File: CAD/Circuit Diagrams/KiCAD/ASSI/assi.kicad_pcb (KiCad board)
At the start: 2 copper layers, 38.1 x 76.2 mm, 24 parts, among them SW2 SW_Push, SW3 SW_Push

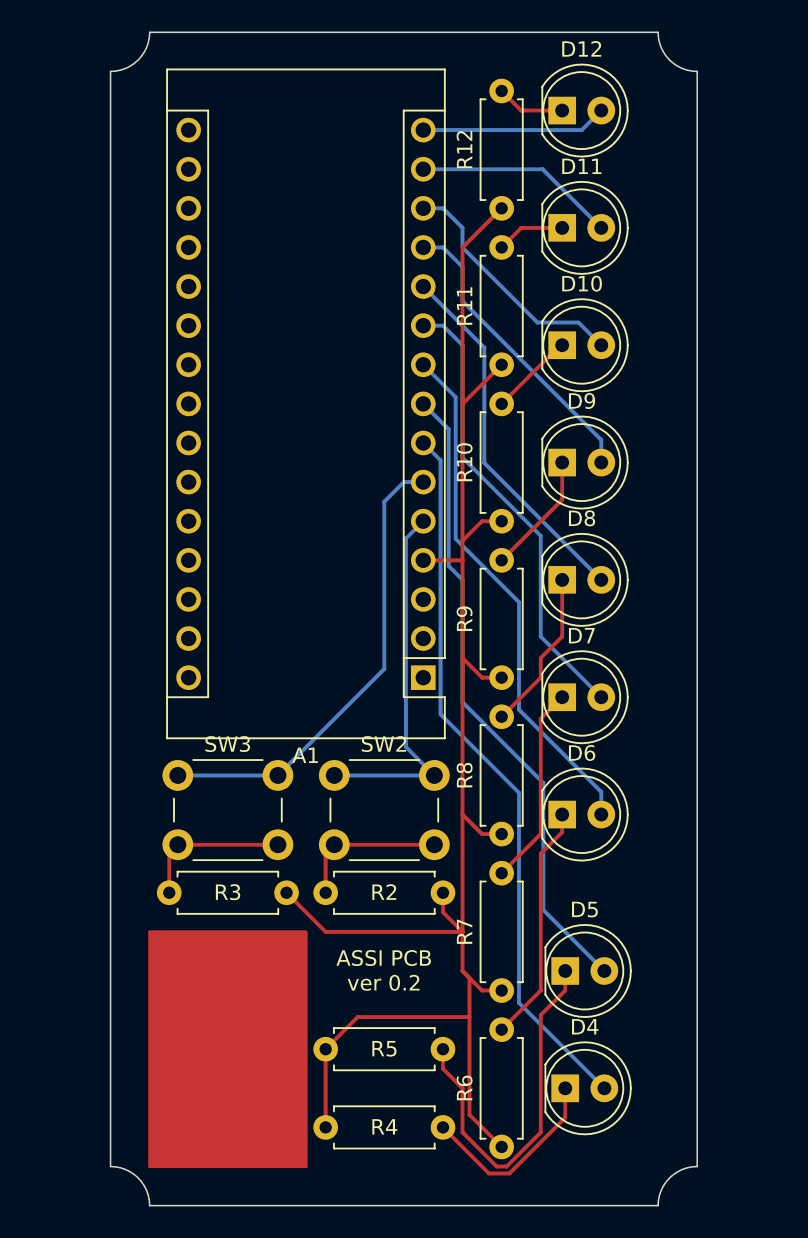
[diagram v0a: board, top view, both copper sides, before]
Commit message: ASSI PCB mountable
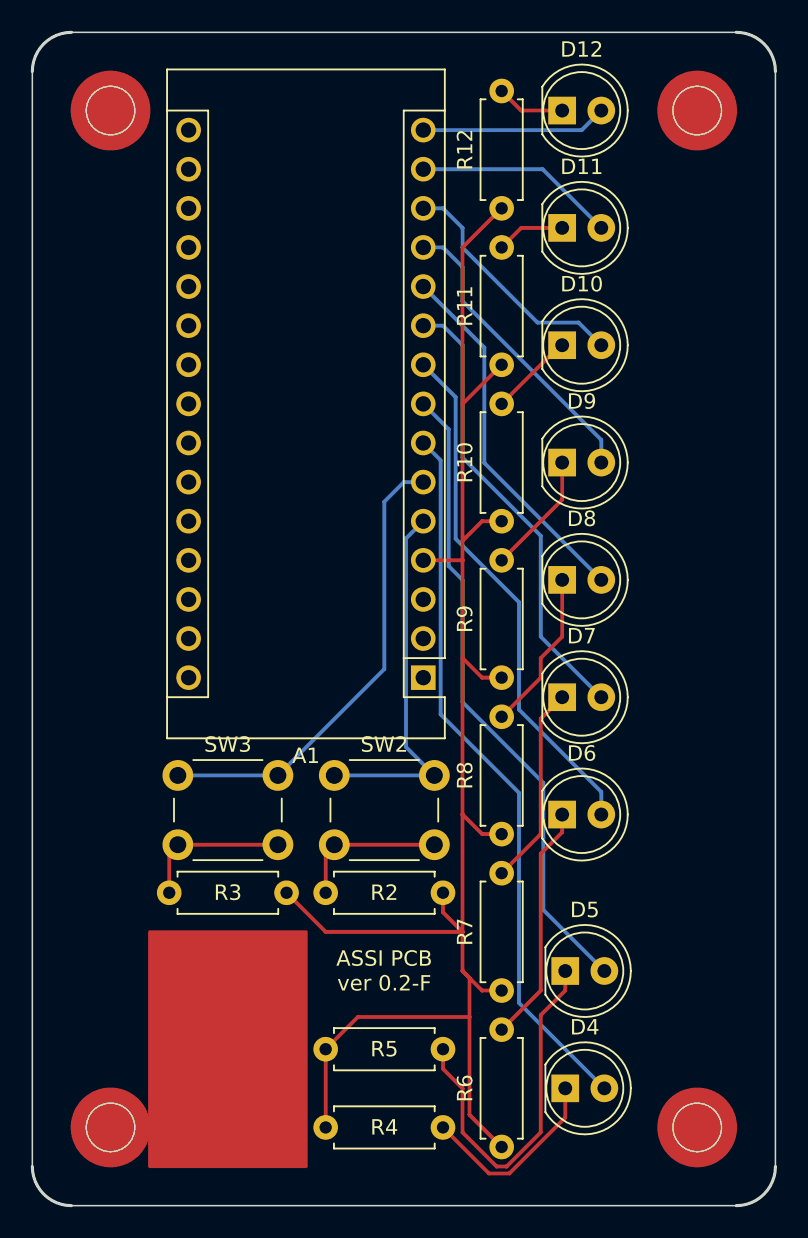
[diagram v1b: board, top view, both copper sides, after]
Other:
- board size 38.1 x 76.2 mm -> 48.3 x 76.2 mm
- board text added: "ASSI PCB ver 0.2-F"
- board text removed: "ASSI PCB ver 0.2"
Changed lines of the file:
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@@
   (setup
     (pad_to_mask_clearance 0)
-    (grid_origin 163.15 125.96)
+    (grid_origin 155.53 70.08)
     (pcbplotparams
       (layerselection 0x00010fc_ffffffff)
@@
     )
   )
+  (gr_circle (center 196.17 138.66) (end 198.71 138.66) (layer "F.Cu") (width 0.1) (fill solid))
+  (gr_circle (center 158.07 72.62) (end 160.61 72.62) (layer "F.Cu") (width 0.1) (fill solid))
   (gr_rect (start 160.61 125.96) (end 170.77 141.2) (layer "F.Cu") (width 0.2) (fill solid))
-  (gr_arc (start 196.17 70.08) (mid 194.373949 69.336051) (end 193.63 67.54) (layer "Edge.Cuts") (width 0.1))
-  (gr_line (start 193.63 67.54) (end 160.61 67.54) (layer "Edge.Cuts") (width 0.1))
-  (gr_arc (start 193.63 143.74) (mid 194.373949 141.943949) (end 196.17 141.2) (layer "Edge.Cuts") (width 0.1))
-  (gr_line (start 160.61 143.74) (end 193.63 143.74) (layer "Edge.Cuts") (width 0.1))
-  (gr_arc (start 160.61 67.54) (mid 159.866051 69.336051) (end 158.07 70.08) (layer "Edge.Cuts") (width 0.1))
-  (gr_line (start 196.17 141.2) (end 196.17 70.08) (layer "Edge.Cuts") (width 0.1))
-  (gr_arc (start 158.07 141.2) (mid 159.866051 141.943949) (end 160.61 143.74) (layer "Edge.Cuts") (width 0.1))
-  (gr_line (start 158.07 70.08) (end 158.07 141.2) (layer "Edge.Cuts") (width 0.1))
-  (gr_text "ASSI PCB\nver 0.2" (at 175.85 128.5) (layer "F.SilkS")
+  (gr_circle (center 196.17 72.62) (end 198.71 72.62) (layer "F.Cu") (width 0.1) (fill solid))
+  (gr_circle (center 158.07 138.66) (end 160.61 138.66) (layer "F.Cu") (width 0.1) (fill solid))
+  (gr_circle (center 196.17 138.66) (end 198.71 138.66) (layer "F.Paste") (width 0.1) (fill solid))
+  (gr_circle (center 158.07 138.66) (end 160.61 138.66) (layer "F.Paste") (width 0.1) (fill solid))
+  (gr_circle (center 158.07 72.62) (end 160.61 72.62) (layer "F.Paste") (width 0.1) (fill solid))
+  (gr_circle (center 196.17 72.62) (end 198.71 72.62) (layer "F.Paste") (width 0.1) (fill solid))
+  (gr_arc (start 198.71 67.54) (mid 200.506051 68.283949) (end 201.25 70.08) (layer "Edge.Cuts") (width 0.2))
+  (gr_circle (center 158.07 138.66) (end 159.645 138.66) (layer "Edge.Cuts") (width 0.1) (fill none))
+  (gr_arc (start 152.99 70.08) (mid 153.733949 68.283949) (end 155.53 67.54) (layer "Edge.Cuts") (width 0.2))
+  (gr_line (start 198.71 67.54) (end 155.53 67.54) (layer "Edge.Cuts") (width 0.1))
+  (gr_circle (center 196.17 138.66) (end 197.745 138.66) (layer "Edge.Cuts") (width 0.1) (fill none))
+  (gr_arc (start 155.53 143.74) (mid 153.733949 142.996051) (end 152.99 141.2) (layer "Edge.Cuts") (width 0.2))
+  (gr_line (start 155.53 143.74) (end 198.71 143.74) (layer "Edge.Cuts") (width 0.1))
+  (gr_arc (start 201.25 141.2) (mid 200.506051 142.996051) (end 198.71 143.74) (layer "Edge.Cuts") (width 0.2))
+  (gr_line (start 201.25 141.2) (end 201.25 70.08) (layer "Edge.Cuts") (width 0.1))
+  (gr_circle (center 158.07 72.62) (end 159.645 72.62) (layer "Edge.Cuts") (width 0.1) (fill none))
+  (gr_circle (center 196.17 72.62) (end 197.745 72.62) (layer "Edge.Cuts") (width 0.1) (fill none))
+  (gr_line (start 152.99 70.08) (end 152.99 141.2) (layer "Edge.Cuts") (width 0.1))
+  (gr_text "ASSI PCB\nver 0.2-F" (at 175.85 128.5) (layer "F.SilkS")
     (effects (font (size 1 1) (thickness 0.15)))
   )
+  (dimension (type aligned) (layer "Edge.Cuts")
+    (pts (xy 152.99 72.62) (xy 158.07 72.62))
+    (height -12.7)
+    (gr_text "5.0800 mm" (at 155.53 58.77) (layer "Edge.Cuts")
+      (effects (font (size 1 1) (thickness 0.15)))
+    )
+    (format (units 3) (units_format 1) (precision 4))
+    (style (thickness 0.1) (arrow_length 1.27) (text_position_mode 0) (extension_height 0.58642) (extension_offset 0.5) keep_text_aligned)
+  )
+  (dimension (type aligned) (layer "Edge.Cuts")
+    (pts (xy 152.99 70.08) (xy 201.25 70.08))
+    (height -12.7)
+    (gr_text "48.2600 mm" (at 177.12 56.23) (layer "Edge.Cuts")
+      (effects (font (size 1 1) (thickness 0.15)))
+    )
+    (format (units 3) (units_format 1) (precision 4))
+    (style (thickness 0.1) (arrow_length 1.27) (text_position_mode 0) (extension_height 0.58642) (extension_offset 0.5) keep_text_aligned)
+  )
+  (dimension (type aligned) (layer "Edge.Cuts")
+    (pts (xy 155.53 70.08) (xy 155.53 67.54))
+    (height -15.24)
+    (gr_text "2.5400 mm" (at 139.14 68.81 90) (layer "Edge.Cuts")
+      (effects (font (size 1 1) (thickness 0.15)))
+    )
+    (format (units 3) (units_format 1) (precision 4))
+    (style (thickness 0.1) (arrow_length 1.27) (text_position_mode 0) (extension_height 0.58642) (extension_offset 0.5) keep_text_aligned)
+  )
+  (dimension (type aligned) (layer "Edge.Cuts")
+    (pts (xy 158.07 72.62) (xy 156.495 72.62))
+    (height 7.62)
+    (gr_text "1.5750 mm" (at 157.2825 63.85) (layer "Edge.Cuts")
+      (effects (font (size 1 1) (thickness 0.15)))
+    )
+    (format (units 3) (units_format 1) (precision 4))
+    (style (thickness 0.1) (arrow_length 1.27) (text_position_mode 0) (extension_height 0.58642) (extension_offset 0.5) keep_text_aligned)
+  )
+  (dimension (type aligned) (layer "Edge.Cuts")
+    (pts (xy 155.53 143.74) (xy 155.53 67.54))
+    (height -10.16)
+    (gr_text "76.2000 mm" (at 144.22 105.64 90) (layer "Edge.Cuts")
+      (effects (font (size 1 1) (thickness 0.15)))
+    )
+    (format (units 3) (units_format 1) (precision 4))
+    (style (thickness 0.1) (arrow_length 1.27) (text_position_mode 0) (extension_height 0.58642) (extension_offset 0.5) keep_text_aligned)
+  )
+  (dimension (type aligned) (layer "Edge.Cuts")
+    (pts (xy 158.07 72.62) (xy 158.07 67.54))
+    (height -7.62)
+    (gr_text "5.0800 mm" (at 149.3 70.08 90) (layer "Edge.Cuts")
+      (effects (font (size 1 1) (thickness 0.15)))
+    )
+    (format (units 3) (units_format 1) (precision 4))
+    (style (thickness 0.1) (arrow_length 1.27) (text_position_mode 0) (extension_height 0.58642) (extension_offset 0.5) keep_text_aligned)
+  )
+  (dimension (type aligned) (layer "Edge.Cuts")
+    (pts (xy 158.07 72.62) (xy 155.53 72.62))
+    (height 10.16)
+    (gr_text "2.5400 mm" (at 156.8 61.31) (layer "Edge.Cuts")
+      (effects (font (size 1 1) (thickness 0.15)))
+    )
+    (format (units 3) (units_format 1) (precision 4))
+    (style (thickness 0.1) (arrow_length 1.27) (text_position_mode 0) (extension_height 0.58642) (extension_offset 0.5) keep_text_aligned)
+  )
   (segment (start 180.93 100.56) (end 182.2 99.29) (width 0.25) (layer "F.Cu") (net 4))

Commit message: Small ASSI PCB fix
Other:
- board text added: "ASSI PCB ver 0.3-F"
- board text removed: "ASSI PCB ver 0.2-F"
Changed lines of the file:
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@@
     )
   )
-  (gr_circle (center 196.17 138.66) (end 198.71 138.66) (layer "F.Cu") (width 0.1) (fill solid))
-  (gr_circle (center 158.07 72.62) (end 160.61 72.62) (layer "F.Cu") (width 0.1) (fill solid))
   (gr_rect (start 160.61 125.96) (end 170.77 141.2) (layer "F.Cu") (width 0.2) (fill solid))
   (gr_circle (center 196.17 72.62) (end 198.71 72.62) (layer "F.Cu") (width 0.1) (fill solid))
+  (gr_circle (center 196.17 138.66) (end 198.71 138.66) (layer "F.Cu") (width 0.1) (fill solid))
   (gr_circle (center 158.07 138.66) (end 160.61 138.66) (layer "F.Cu") (width 0.1) (fill solid))
-  (gr_circle (center 196.17 138.66) (end 198.71 138.66) (layer "F.Paste") (width 0.1) (fill solid))
-  (gr_circle (center 158.07 138.66) (end 160.61 138.66) (layer "F.Paste") (width 0.1) (fill solid))
-  (gr_circle (center 158.07 72.62) (end 160.61 72.62) (layer "F.Paste") (width 0.1) (fill solid))
-  (gr_circle (center 196.17 72.62) (end 198.71 72.62) (layer "F.Paste") (width 0.1) (fill solid))
+  (gr_circle (center 158.07 72.62) (end 160.61 72.62) (layer "F.Cu") (width 0.1) (fill solid))
+  (gr_circle (center 158.07 138.66) (end 160.61 138.66) (layer "B.Cu") (width 0.1) (fill solid))
+  (gr_circle (center 196.17 72.62) (end 198.71 72.62) (layer "B.Cu") (width 0.1) (fill solid))
+  (gr_circle (center 158.07 72.62) (end 160.61 72.62) (layer "B.Cu") (width 0.1) (fill solid))
+  (gr_circle (center 196.17 138.66) (end 198.71 138.66) (layer "B.Cu") (width 0.1) (fill solid))
+  (gr_circle (center 158.07 72.62) (end 160.61 72.62) (layer "B.Mask") (width 0.1) (fill solid))
+  (gr_circle (center 196.17 72.62) (end 198.71 72.62) (layer "B.Mask") (width 0.1) (fill solid))
+  (gr_circle (center 196.17 138.66) (end 198.71 138.66) (layer "B.Mask") (width 0.1) (fill solid))
+  (gr_circle (center 158.07 138.66) (end 160.61 138.66) (layer "B.Mask") (width 0.1) (fill solid))
+  (gr_circle (center 158.07 138.66) (end 160.61 138.66) (layer "F.Mask") (width 0.1) (fill solid))
+  (gr_circle (center 196.17 138.66) (end 198.71 138.66) (layer "F.Mask") (width 0.1) (fill solid))
+  (gr_circle (center 196.17 72.62) (end 198.71 72.62) (layer "F.Mask") (width 0.1) (fill solid))
+  (gr_circle (center 158.07 72.62) (end 160.61 72.62) (layer "F.Mask") (width 0.1) (fill solid))
+  (gr_circle (center 158.07 138.66) (end 159.645 138.66) (layer "Edge.Cuts") (width 0.1) (fill none))
   (gr_arc (start 198.71 67.54) (mid 200.506051 68.283949) (end 201.25 70.08) (layer "Edge.Cuts") (width 0.2))
-  (gr_circle (center 158.07 138.66) (end 159.645 138.66) (layer "Edge.Cuts") (width 0.1) (fill none))
-  (gr_arc (start 152.99 70.08) (mid 153.733949 68.283949) (end 155.53 67.54) (layer "Edge.Cuts") (width 0.2))
+  (gr_circle (center 158.07 72.62) (end 159.645 72.62) (layer "Edge.Cuts") (width 0.1) (fill none))
   (gr_line (start 198.71 67.54) (end 155.53 67.54) (layer "Edge.Cuts") (width 0.1))
-  (gr_circle (center 196.17 138.66) (end 197.745 138.66) (layer "Edge.Cuts") (width 0.1) (fill none))
   (gr_arc (start 155.53 143.74) (mid 153.733949 142.996051) (end 152.99 141.2) (layer "Edge.Cuts") (width 0.2))
   (gr_line (start 155.53 143.74) (end 198.71 143.74) (layer "Edge.Cuts") (width 0.1))
+  (gr_arc (start 152.99 70.08) (mid 153.733949 68.283949) (end 155.53 67.54) (layer "Edge.Cuts") (width 0.2))
+  (gr_line (start 201.25 141.2) (end 201.25 70.08) (layer "Edge.Cuts") (width 0.1))
+  (gr_circle (center 196.17 72.62) (end 197.745 72.62) (layer "Edge.Cuts") (width 0.1) (fill none))
+  (gr_circle (center 196.17 138.66) (end 197.745 138.66) (layer "Edge.Cuts") (width 0.1) (fill none))
   (gr_arc (start 201.25 141.2) (mid 200.506051 142.996051) (end 198.71 143.74) (layer "Edge.Cuts") (width 0.2))
-  (gr_line (start 201.25 141.2) (end 201.25 70.08) (layer "Edge.Cuts") (width 0.1))
-  (gr_circle (center 158.07 72.62) (end 159.645 72.62) (layer "Edge.Cuts") (width 0.1) (fill none))
-  (gr_circle (center 196.17 72.62) (end 197.745 72.62) (layer "Edge.Cuts") (width 0.1) (fill none))
   (gr_line (start 152.99 70.08) (end 152.99 141.2) (layer "Edge.Cuts") (width 0.1))
-  (gr_text "ASSI PCB\nver 0.2-F" (at 175.85 128.5) (layer "F.SilkS")
+  (gr_text "ASSI PCB\nver 0.3-F" (at 175.85 128.5) (layer "F.SilkS")
     (effects (font (size 1 1) (thickness 0.15)))
   )
@@
   )
   (dimension (type aligned) (layer "Edge.Cuts")
-    (pts (xy 155.53 143.74) (xy 155.53 67.54))
+    (pts (xy 158.07 143.74) (xy 158.07 67.54))
     (height -10.16)
-    (gr_text "76.2000 mm" (at 144.22 105.64 90) (layer "Edge.Cuts")
+    (gr_text "76.2000 mm" (at 146.76 105.64 90) (layer "Edge.Cuts")
       (effects (font (size 1 1) (thickness 0.15)))
     )
